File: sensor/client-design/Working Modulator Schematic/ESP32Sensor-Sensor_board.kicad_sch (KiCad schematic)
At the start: 16 parts, among them U1 ESP32-DEVKITC-32D, U7 AD620ARZ-REEL7, U8 AD630ARZ

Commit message: Breadboard Update 1
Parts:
- added C4, C5: 100nF, Capacitor_SMD:C_0402_1005Metric, symbol Device:C
- added R10: 6.66K, Resistor_SMD:R_0402_1005Metric, symbol Device:R
- added R11: 7K, Resistor_SMD:R_0402_1005Metric, symbol Device:R
- added R12: 20k, Resistor_SMD:R_0402_1005Metric, symbol Device:R
- added R8, R9: 1M, Resistor_SMD:R_0402_1005Metric, symbol Device:R
- added U2: OP27GSZ-REEL7, footprints:R_8_ADI, symbol OP27:OP27GSZ-REEL7
- C3: value C -> 100nF
- R5: value R -> 10k
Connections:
- net +Vs_For_Lock_in: now also U2.7 (V+)
- net -Vs_For_Lock_in: now also U2.4 (V-)
- new net: R10.1, R11.1, U2.2 (-IN)
- new net: C5.1, R9.2, U2.3 (+IN)
- new net: R12.1, U2.6 (OUT)
- new net: C4.1, R8.2, R9.1
- new net Sensor_Analog: R11.2, R12.2
- new net Sensor_GND: C4.2, C5.2, R10.2
- no-connect marks 7 -> 10

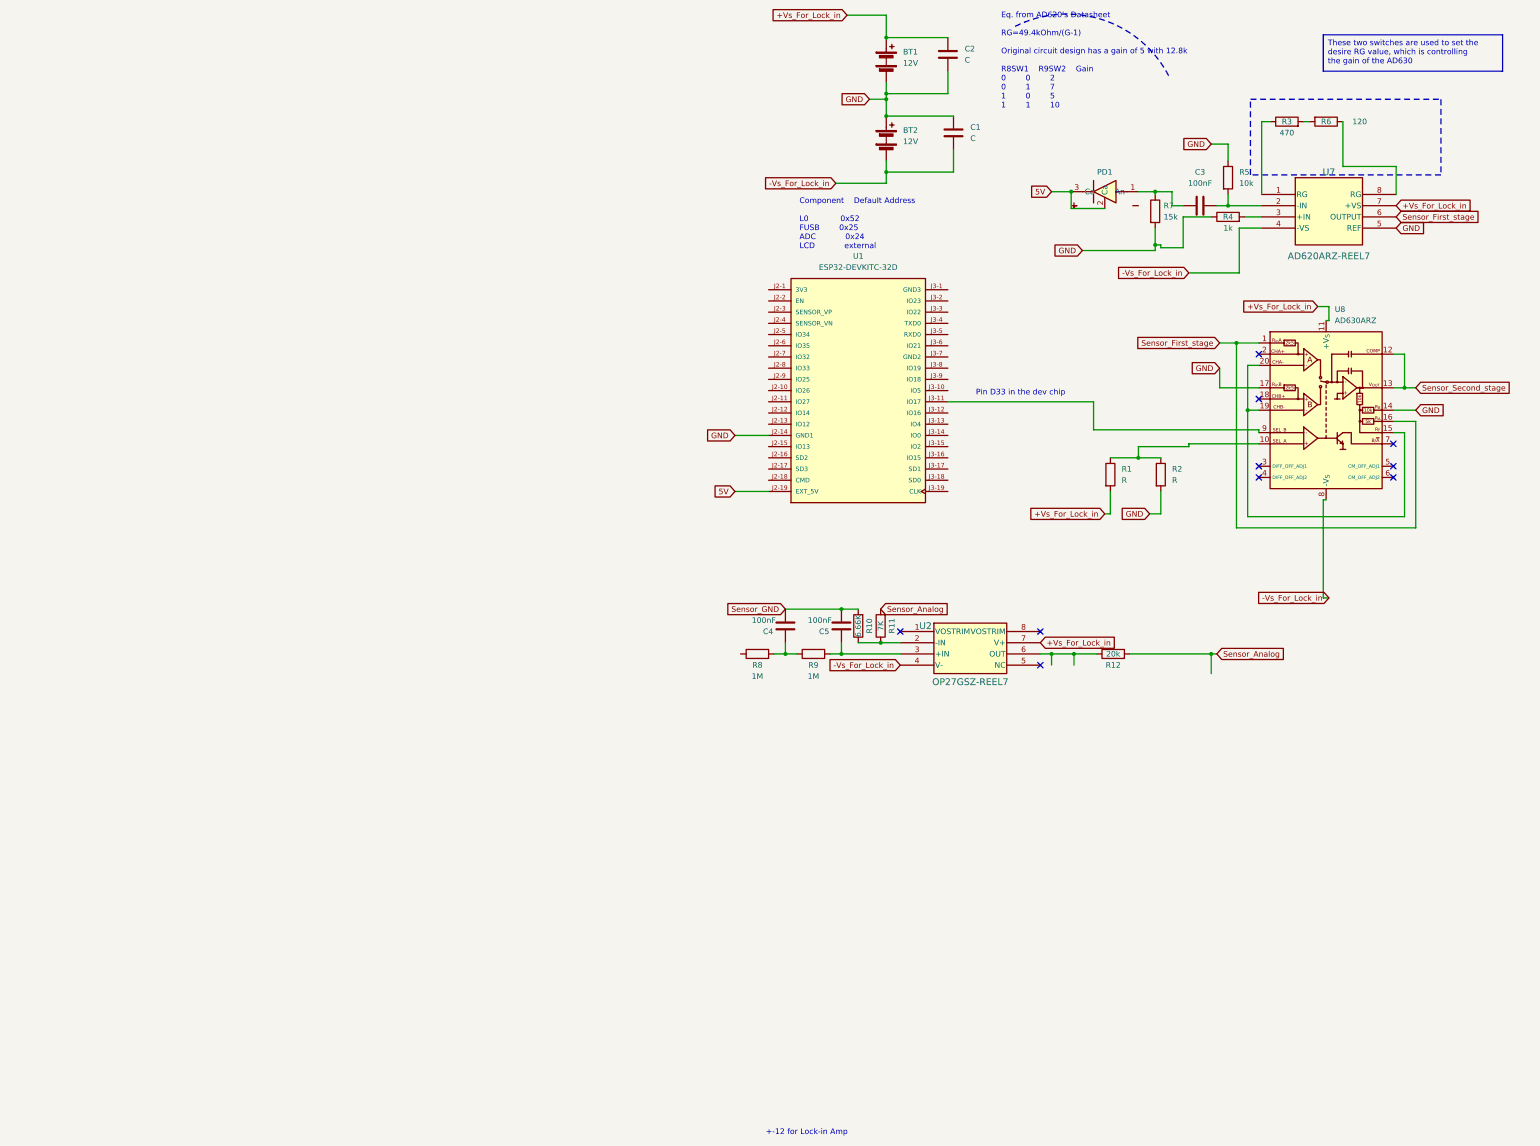
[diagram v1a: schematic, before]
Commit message: Breadboard Schematic update
finished output op27 circuit
Added all the resistor values
added all decoupling capacitors
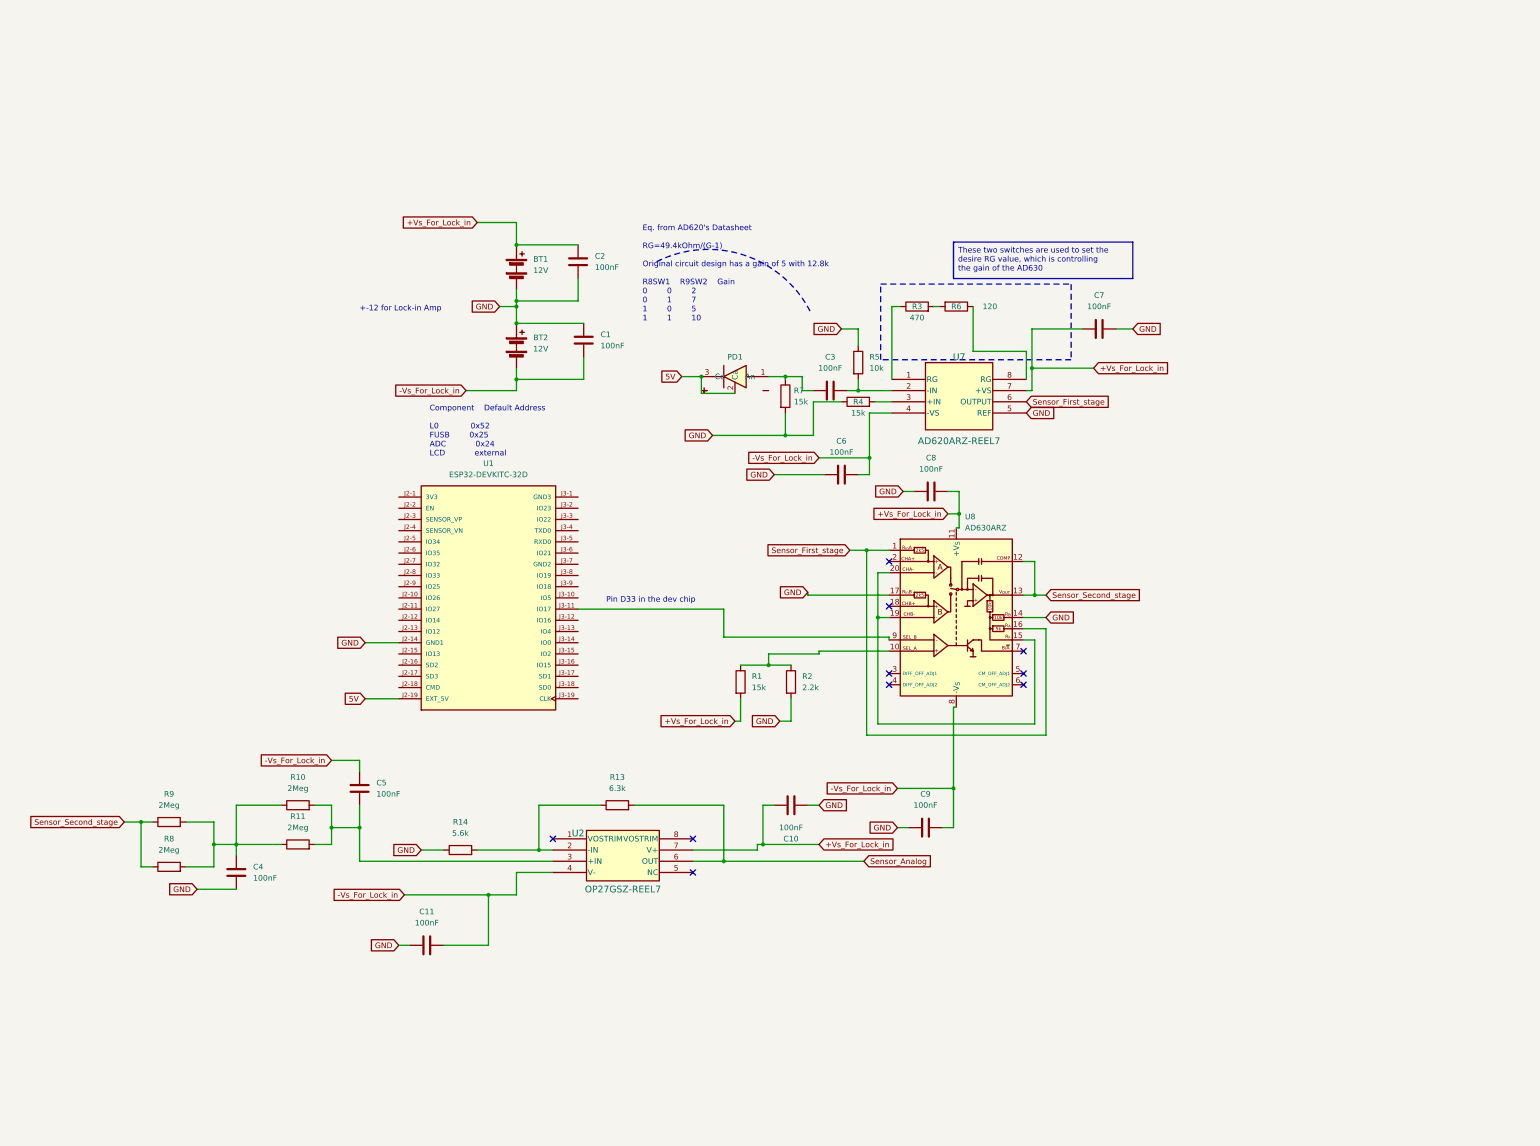
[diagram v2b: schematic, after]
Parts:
- removed R12: 20k, Resistor_SMD:R_0402_1005Metric, symbol Device:R
- added C10, C11, C6, C7, C8, C9: 100nF, symbol Device:C
- added R13: 6.3k, symbol Device:R
- added R14: 5.6k, symbol Device:R
- C1, C2: value C -> 100nF
- C4, C5: footprint Capacitor_SMD:C_0402_1005Metric -> (none)
- R1: value R -> 15k
- R10: value 6.66K -> 2Meg; footprint Resistor_SMD:R_0402_1005Metric -> (none)
- R11: value 7K -> 2Meg; footprint Resistor_SMD:R_0402_1005Metric -> (none)
- R2: value R -> 2.2k
- R4: value 1k -> 15k
- R8, R9: value 1M -> 2Meg; footprint Resistor_SMD:R_0402_1005Metric -> (none)
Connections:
- net +Vs_For_Lock_in: now also C10.2, C7.1, C8.2
- net -Vs_For_Lock_in: now also C5.1, C11.2, C6.2, C9.2
- net GND: now also C4.2, C10.1, C11.1, C6.1, C7.2, C8.1, C9.1, R14.1
- net Sensor_Analog: now also U2.6 (OUT), R13.2; no longer R11.2
- net Sensor_Second_stage: now also R8.1, R9.1
- net at R10.1, R11.1: now also C4.1, R8.2, R9.2; no longer U2.2 (-IN)
- net Sensor_GND: no longer names the net of C5.2, R10.2
- net Sensor_GND: now also R11.2, U2.3 (+IN); no longer C4.2
- new net: R13.1, R14.2, U2.2 (-IN)
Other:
- moved on the sheet: BT1, BT2, C1, C2, C3, PD1, R1, R2, R3, R4, R5, R6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
